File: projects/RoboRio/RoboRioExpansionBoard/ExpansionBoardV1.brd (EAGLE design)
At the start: 100.3 x 80.3 mm, 82 parts, among them Q1 5MHz

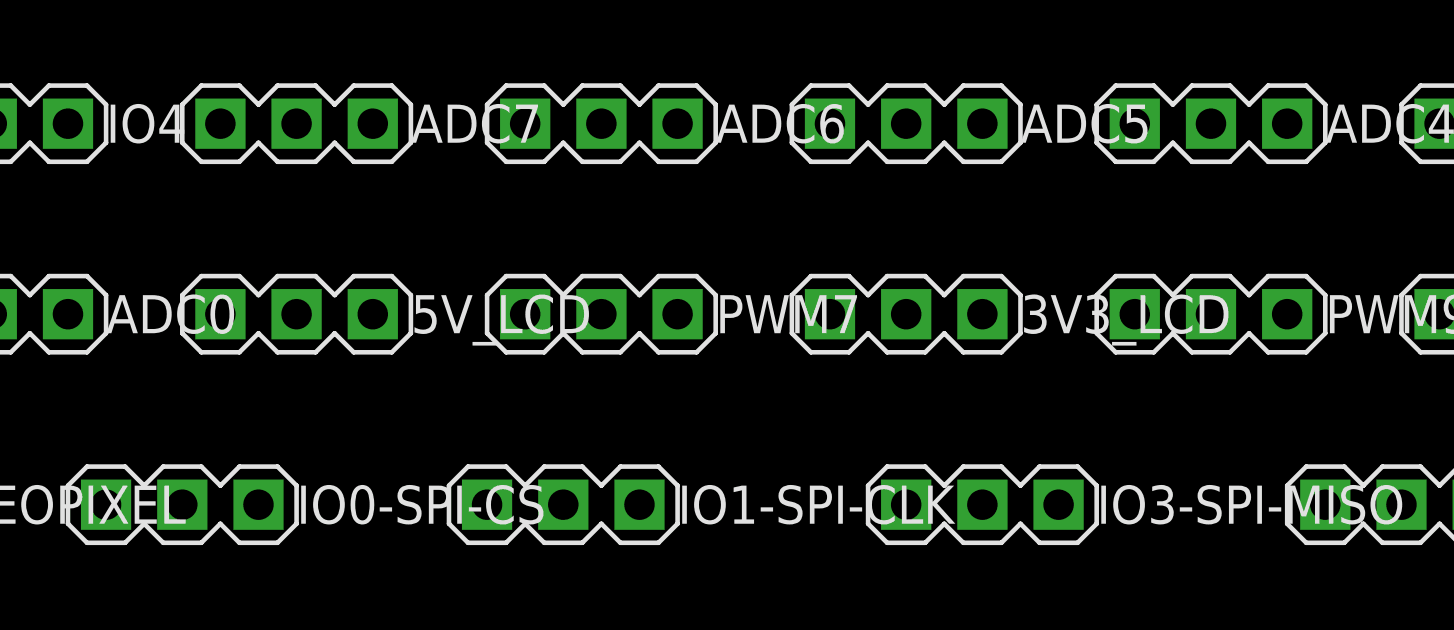
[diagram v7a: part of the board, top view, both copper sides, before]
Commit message: Updated PWM pass-throughs to be a separate bus
also removed 3.3v connection for LCD so there is only one
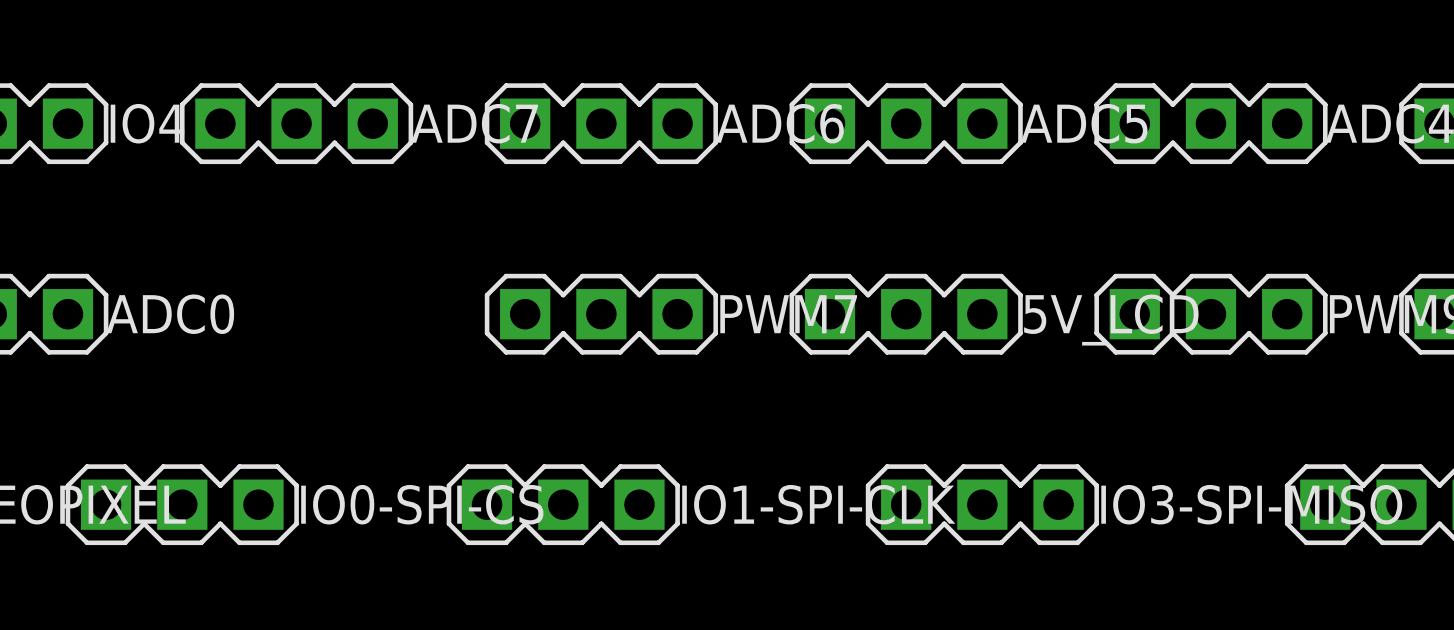
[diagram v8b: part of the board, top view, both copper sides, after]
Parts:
- removed 3V3_LCD: (no value), con-lstb-modified:MA03-1
- R5: value 10k -> 150
- moved 5V_LCD 20.3 mm to (-38.1, 90.2)
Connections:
- net DIO0 renamed PWM0
- net DIO1 renamed PWM1
- net DIO10 renamed PWM6
- net DIO11 renamed PWM7
- net DIO12 renamed PWM8
- net DIO13 renamed PWM9
- net DIO2 renamed PWM2
- net DIO3 renamed PWM3
- net DIO9 renamed PWM5
- removed net DIO8: PWM4.1, U$1.27, U$2.27
- removed net N$15: 5V_LCD.3, LEVELSHIFTER.5
- removed net N$16: C13.2
- removed net N$18: AI1.2, AI2.2, AI3.2, AI4.2, AI5.2, AIO.2
- new net PWM4: U$1.27, U$2.27
- net +3V3: no longer 3V3_LCD.2, LEVELSHIFTER.7
- net +5V: now also AI1.2, AI2.2, AI3.2, AI4.2, AI5.2, AIO.2
- net GND: now also ADC.10, C13.2; no longer 3V3_LCD.1
- net IO12: no longer ADC.10
- net IO5: now also 5V_LCD.3; no longer 3V3_LCD.3, LEVELSHIFTER.6
